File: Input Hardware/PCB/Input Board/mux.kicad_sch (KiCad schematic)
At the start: 40 parts

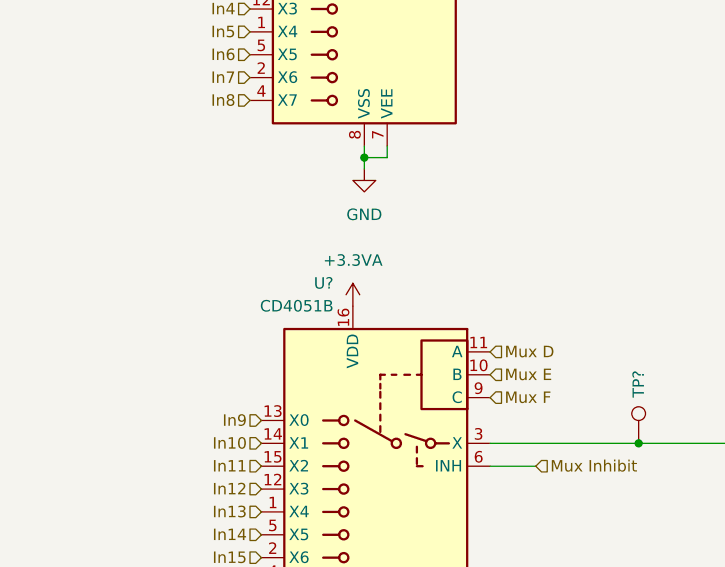
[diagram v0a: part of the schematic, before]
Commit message: Fix footprints
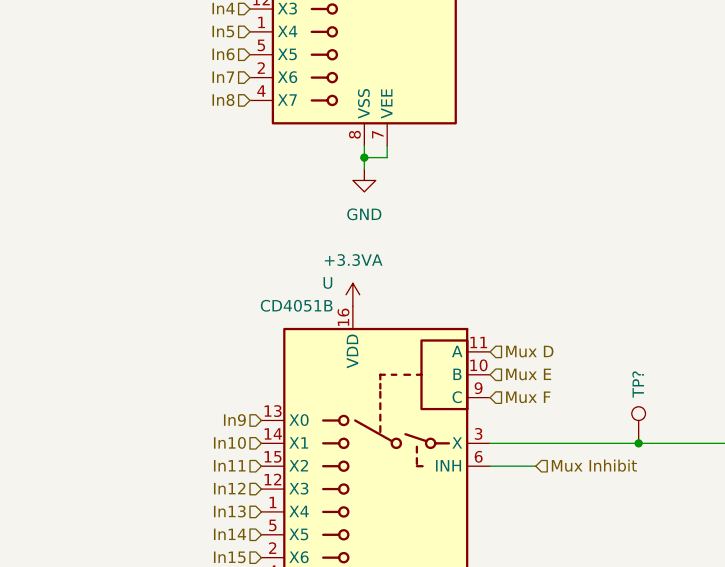
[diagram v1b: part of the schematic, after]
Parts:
- removed U? (x2): CD4051B, symbol Analog_Switch:CD4051B
- added U, U?: CD4051B, Package_SO:SOIC-16_3.9x9.9mm_P1.27mm, symbol Analog_Switch:CD4051B
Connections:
- net +3.3VA: now also U.16 (VDD), U?.16 (VDD)
- net GND: now also U.7 (VEE), U.8 (VSS), U?.7 (VEE), U?.8 (VSS)
- net In1: now also U?.13 (X0)
- net In10: now also U.14 (X1)
- net In11: now also U.15 (X2)
- net In12: now also U.12 (X3)
- net In13: now also U.1 (X4)
- net In14: now also U.5 (X5)
- net In15: now also U.2 (X6)
- net In16: now also U.4 (X7)
- net In2: now also U?.14 (X1)
- net In3: now also U?.15 (X2)
- net In4: now also U?.12 (X3)
- net In5: now also U?.1 (X4)
- net In6: now also U?.5 (X5)
- net In7: now also U?.2 (X6)
- net In8: now also U?.4 (X7)
- net In9: now also U.13 (X0)
- net Mux A: now also U?.11 (A)
- net Mux B: now also U?.10 (B)
- net Mux C: now also U?.9 (C)
- net Mux D: now also U.11 (A)
- net Mux E: now also U.10 (B)
- net Mux F: now also U.9 (C)
- net Mux Inhibit: now also U.6 (INH), U?.6 (INH)
- net at R?.1, TP?.1: now also U?.3 (X)
- net at R?.1, TP?.1: now also U.3 (X)
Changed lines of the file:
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@@
-	)
-	(symbol
-		(lib_id "Analog_Switch:CD4051B")
-		(at 59.69 43.18 0)
-		(mirror y)
-		(unit 1)
-		(exclude_from_sim no)
-		(in_bom yes)
-		(on_board yes)
-		(dnp no)
-		(property "Reference" "U?"
-			(at 55.0067 22.86 0)
-			(effects
-				(font
-					(size 1.27 1.27)
-				)
-				(justify left)
-			)
-		)
-		(property "Value" "CD4051B"
-			(at 55.0067 25.4 0)
-			(effects
-				(font
-					(size 1.27 1.27)
-				)
-				(justify left)
-			)
-		)
-		(property "Footprint" ""
-			(at 55.88 62.23 0)
-			(effects
-				(font
-					(size 1.27 1.27)
-				)
-				(justify left)
-				(hide yes)
-			)
-		)
-		(property "Datasheet" "http://www.ti.com/lit/ds/symlink/cd4052b.pdf"
-			(at 60.198 40.64 0)
-			(effects
-				(font
-					(size 1.27 1.27)
-				)
-				(hide yes)
-			)
-		)
-		(property "Description" "CMOS single 8-channel analog multiplexer demultiplexer, TSSOP-16/DIP-16/SOIC-16"
-			(at 59.69 43.18 0)
-			(effects
-				(font
-					(size 1.27 1.27)
-				)
-				(hide yes)
-			)
-		)
-		(pin "11"
-		)
-		(pin "4"
-		)
-		(pin "5"
-		)
-		(pin "14"
-		)
-		(pin "16"
-		)
-		(pin "7"
-		)
-		(pin "6"
-		)
-		(pin "3"
-		)
-		(pin "9"
-		)
-		(pin "8"
-		)
-		(pin "1"
-		)
-		(pin "10"
-		)
-		(pin "12"
-		)
-		(pin "15"
-		)
-		(pin "13"
-		)
-		(pin "2"
-		)
-		(instances
-			(project "Input Board"
-				(path "/198ad8d1-66e3-4deb-889c-1af2b81e67c3/99a15fca-8895-44e6-9a10-1270216dbd6f"
-					(reference "U?")
-					(unit 1)
-				)
-				(path "/198ad8d1-66e3-4deb-889c-1af2b81e67c3/ccfc9974-2797-4490-9af9-c0259e48d54a"
-					(reference "U?")
-					(unit 1)
-				)
-			)
-		)
 	)
 	(symbol
@@
 	)
 	(symbol
+		(lib_id "Analog_Switch:CD4051B")
+		(at 59.69 43.18 0)
+		(mirror y)
+		(unit 1)
+		(exclude_from_sim no)
+		(in_bom yes)
+		(on_board yes)
+		(dnp no)
+		(property "Reference" "U?"
+			(at 55.0067 22.86 0)
+			(effects
+				(font
+					(size 1.27 1.27)
+				)
+				(justify left)
+			)
+		)
+		(property "Value" "CD4051B"
+			(at 55.0067 25.4 0)
+			(effects
+				(font
+					(size 1.27 1.27)
+				)
+				(justify left)
+			)
+		)
+		(property "Footprint" "Package_SO:SOIC-16_3.9x9.9mm_P1.27mm"
+			(at 55.88 62.23 0)
+			(effects
+				(font
+					(size 1.27 1.27)
+				)
+				(justify left)
+				(hide yes)
+			)
+		)
+		(property "Datasheet" "http://www.ti.com/lit/ds/symlink/cd4052b.pdf"
+			(at 60.198 40.64 0)
+			(effects
+				(font
+					(size 1.27 1.27)
+				)
+				(hide yes)
+			)
+		)
+		(property "Description" "CMOS single 8-channel analog multiplexer demultiplexer, TSSOP-16/DIP-16/SOIC-16"
+			(at 59.69 43.18 0)
+			(effects
+				(font
+					(size 1.27 1.27)
+				)
+				(hide yes)
+			)
+		)
+		(pin "8"
+		)
+		(pin "14"
+		)
+		(pin "13"
+		)
+		(pin "4"
+		)
+		(pin "2"
+		)
+		(pin "9"
+		)
+		(pin "10"
+		)
+		(pin "1"
+		)
+		(pin "15"
+		)
+		(pin "6"
+		)
+		(pin "16"
+		)
+		(pin "3"
+		)
+		(pin "7"
+		)
+		(pin "12"
+		)
+		(pin "5"
+		)
+		(pin "11"
+		)
+		(instances
+			(project "Input Board"
+				(path "/198ad8d1-66e3-4deb-889c-1af2b81e67c3/99a15fca-8895-44e6-9a10-1270216dbd6f"
+					(reference "U?")
+					(unit 1)
+				)
+				(path "/198ad8d1-66e3-4deb-889c-1af2b81e67c3/ccfc9974-2797-4490-9af9-c0259e48d54a"
+					(reference "U?")
+					(unit 1)
+				)
+			)
+		)
+	)
+	(symbol
 		(lib_id "power:+3.3VA")
 		(at 58.42 78.74 0)
@@
 	)
 	(symbol
+		(lib_id "Analog_Switch:CD4051B")
+		(at 60.96 96.52 0)
+		(mirror y)
+		(unit 1)
+		(exclude_from_sim no)
+		(in_bom yes)
+		(on_board yes)
+		(dnp no)
+		(property "Reference" "U"
+			(at 56.2767 76.2 0)
+			(effects
+				(font
+					(size 1.27 1.27)
+				)
+				(justify left)
+			)
+		)
+		(property "Value" "CD4051B"
+			(at 56.2767 78.74 0)
+			(effects
+				(font
+					(size 1.27 1.27)
+				)
+				(justify left)
+			)
+		)
+		(property "Footprint" "Package_SO:SOIC-16_3.9x9.9mm_P1.27mm"
+			(at 57.15 115.57 0)
+			(effects
+				(font
+					(size 1.27 1.27)
+				)
+				(justify left)
+				(hide yes)
+			)
+		)
+		(property "Datasheet" "http://www.ti.com/lit/ds/symlink/cd4052b.pdf"
+			(at 61.468 93.98 0)
+			(effects
+				(font
+					(size 1.27 1.27)
+				)
+				(hide yes)
+			)
+		)
+		(property "Description" "CMOS single 8-channel analog multiplexer demultiplexer, TSSOP-16/DIP-16/SOIC-16"
+			(at 60.96 96.52 0)
+			(effects
+				(font
+					(size 1.27 1.27)
+				)
+				(hide yes)
+			)
+		)
+		(pin "8"
+		)
+		(pin "14"
+		)
+		(pin "13"
+		)
+		(pin "4"
+		)
+		(pin "2"
+		)
+		(pin "9"
+		)
+		(pin "10"
+		)
+		(pin "1"
+		)
+		(pin "15"
+		)
+		(pin "6"
+		)
+		(pin "16"
+		)
+		(pin "3"
+		)
+		(pin "7"
+		)
+		(pin "12"
+		)
+		(pin "5"
+		)
+		(pin "11"
+		)
+		(instances
+			(project ""
+				(path "/198ad8d1-66e3-4deb-889c-1af2b81e67c3/ccfc9974-2797-4490-9af9-c0259e48d54a"
+					(reference "U?")
+					(unit 1)
+				)
+			)
+		)
+	)
+	(symbol
 		(lib_id "Device:R")
 		(at 149.86 49.53 0)
@@
 					(unit 1)
 				)
-			)
-		)
-	)
-	(symbol
-		(lib_id "Analog_Switch:CD4051B")
-		(at 60.96 96.52 0)
-		(mirror y)
-		(unit 1)
-		(exclude_from_sim no)
-		(in_bom yes)
-		(on_board yes)
-		(dnp no)
-		(property "Reference" "U?"
-			(at 56.2767 76.2 0)
-			(effects
-				(font
-					(size 1.27 1.27)
-				)
-				(justify left)
-			)
-		)
-		(property "Value" "CD4051B"
-			(at 56.2767 78.74 0)
-			(effects
-				(font
-					(size 1.27 1.27)
-				)
-				(justify left)
-			)
-		)
-		(property "Footprint" ""
-			(at 57.15 115.57 0)
-			(effects
-				(font
-					(size 1.27 1.27)
-				)
-				(justify left)
-				(hide yes)
-			)
-		)
-		(property "Datasheet" "http://www.ti.com/lit/ds/symlink/cd4052b.pdf"
-			(at 61.468 93.98 0)
-			(effects
-				(font
-					(size 1.27 1.27)
-				)
-				(hide yes)
-			)
-		)
-		(property "Description" "CMOS single 8-channel analog multiplexer demultiplexer, TSSOP-16/DIP-16/SOIC-16"
-			(at 60.96 96.52 0)
-			(effects
-				(font
-					(size 1.27 1.27)
-				)
-				(hide yes)
-			)
-		)
-		(pin "11"
-		)
-		(pin "4"
-		)
-		(pin "5"
-		)
-		(pin "14"
-		)
-		(pin "16"
-		)
-		(pin "7"
-		)
-		(pin "6"
-		)
-		(pin "3"
-		)
-		(pin "9"
-		)
-		(pin "8"
-		)
-		(pin "1"
-		)
-		(pin "10"
-		)
-		(pin "12"
-		)
-		(pin "15"
-		)
-		(pin "13"
-		)
-		(pin "2"
-		)
-		(instances
-			(project "Input Board"
-				(path "/198ad8d1-66e3-4deb-889c-1af2b81e67c3/99a15fca-8895-44e6-9a10-1270216dbd6f"
-					(reference "U?")
-					(unit 1)
-				)
-				(path "/198ad8d1-66e3-4deb-889c-1af2b81e67c3/ccfc9974-2797-4490-9af9-c0259e48d54a"
-					(reference "U?")
-					(unit 1)
-				)

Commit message: Fix files idc
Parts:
- gave numbers to parts that had none: 35
- renumbered U to U703

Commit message: Filter Amplifier Layout
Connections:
- net In10: now also U703.12 (X3); no longer U703.14 (X1)
- net In12: now also U703.14 (X1); no longer U703.12 (X3)
- net In13: now also U703.4 (X7); no longer U703.1 (X4)
- net In16: now also U703.1 (X4); no longer U703.4 (X7)
- net In2: now also U702.12 (X3); no longer U702.14 (X1)
- net In4: now also U702.14 (X1); no longer U702.12 (X3)
- net In5: now also U702.4 (X7); no longer U702.1 (X4)
- net In8: now also U702.1 (X4); no longer U702.4 (X7)
- net at R715.1, R716.2: now also U701.9 (-); no longer U701.13 (-)
- net at R712.1, R715.2, R718.2: now also U701.8; no longer U701.14
- net at C711.2, R710.2: now also U701.10 (+); no longer U701.12 (+)
- net at R707.1, R708.2: now also U701.13 (-); no longer U701.9 (-)
- net at C707.2, C709.1, R707.2: now also U701.14; no longer U701.8
- net at C705.1, R704.2: now also U701.12 (+); no longer U701.10 (+)
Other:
- moved on the sheet: U701C, U701D
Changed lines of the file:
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@@
 	(hierarchical_label "In10"
 		(shape input)
-		(at 48.26 93.98 180)
+		(at 48.26 99.06 180)
 		(effects
 			(font
@@
 	(hierarchical_label "In16"
 		(shape input)
-		(at 48.26 109.22 180)
+		(at 48.26 101.6 180)
 		(effects
 			(font
@@
 	(hierarchical_label "In4"
 		(shape input)
-		(at 46.99 45.72 180)
+		(at 46.99 40.64 180)
 		(effects
 			(font
@@
 	(hierarchical_label "In2"
 		(shape input)
-		(at 46.99 40.64 180)
+		(at 46.99 45.72 180)
 		(effects
 			(font
@@
 	(hierarchical_label "In8"
 		(shape input)
-		(at 46.99 55.88 180)
+		(at 46.99 48.26 180)
 		(effects
 			(font
@@
 	(hierarchical_label "In12"
 		(shape input)
-		(at 48.26 99.06 180)
+		(at 48.26 93.98 180)
 		(effects
 			(font
@@
 	(hierarchical_label "In13"
 		(shape input)
-		(at 48.26 101.6 180)
+		(at 48.26 109.22 180)
 		(effects
 			(font
@@
 	(hierarchical_label "In5"
 		(shape input)
-		(at 46.99 48.26 180)
+		(at 46.99 55.88 180)
 		(effects
 			(font
@@
 	(symbol
 		(lib_id "Device:Opamp_Quad")
-		(at 140.97 96.52 0)
+		(at 207.01 96.52 0)
 		(unit 3)
 		(exclude_from_sim no)
@@
 		(fields_autoplaced yes)
 		(property "Reference" "U701"
-			(at 140.97 86.36 0)
+			(at 207.01 86.36 0)
 			(effects
 				(font
@@
 		)
 		(property "Value" "ADA4891"
-			(at 140.97 88.9 0)
+			(at 207.01 88.9 0)
 			(effects
 				(font
@@
 		)
 		(property "Footprint" "Package_SO:SOIC-14_3.9x8.7mm_P1.27mm"
-			(at 153.67 96.52 0)
+			(at 219.71 96.52 0)
 			(effects
 				(font
@@
 		)
 		(property "Datasheet" "~"
-			(at 140.97 96.52 0)
+			(at 207.01 96.52 0)
 			(effects
 				(font
@@
 		)
 		(property "Description" "Quad operational amplifier"
-			(at 140.97 96.52 0)
+			(at 207.01 96.52 0)
 			(effects
 				(font
@@
 		)
 		(property "Sim.Library" "${KICAD9_SYMBOL_DIR}/Simulation_SPICE.sp"
-			(at 140.97 96.52 0)
+			(at 207.01 96.52 0)
 			(effects
 				(font
@@
 		)
 		(property "Sim.Name" "kicad_builtin_opamp_quad"
-			(at 140.97 96.52 0)
+			(at 207.01 96.52 0)
 			(effects
 				(font
@@
 		)
 		(property "Sim.Device" "SUBCKT"
-			(at 140.97 96.52 0)
+			(at 207.01 96.52 0)
 			(effects
 				(font
@@
 		)
 		(property "Sim.Pins" "1=out1 2=in1- 3=in1+ 4=vcc 5=in2+ 6=in2- 7=out2 8=out3 9=in3- 10=in3+ 11=vee 12=in4+ 13=in4- 14=out4"
-			(at 140.97 96.52 0)
+			(at 207.01 96.52 0)
 			(effects
 				(font
@@
 	(symbol
 		(lib_id "Device:Opamp_Quad")
-		(at 207.01 96.52 0)
+		(at 140.97 96.52 0)
 		(unit 4)
 		(exclude_from_sim no)
@@
 		(fields_autoplaced yes)
 		(property "Reference" "U701"
-			(at 207.01 86.36 0)
+			(at 140.97 86.36 0)
 			(effects
 				(font
@@
 		)
 		(property "Value" "ADA4891"
-			(at 207.01 88.9 0)
+			(at 140.97 88.9 0)
 			(effects
 				(font
@@
 		)
 		(property "Footprint" "Package_SO:SOIC-14_3.9x8.7mm_P1.27mm"
-			(at 219.71 96.52 0)
+			(at 153.67 96.52 0)
 			(effects
 				(font
@@
 		)
 		(property "Datasheet" "~"
-			(at 207.01 96.52 0)
+			(at 140.97 96.52 0)
 			(effects
 				(font
@@
 		)
 		(property "Description" "Quad operational amplifier"
-			(at 207.01 96.52 0)
+			(at 140.97 96.52 0)
 			(effects
 				(font
@@
 		)
 		(property "Sim.Library" "${KICAD9_SYMBOL_DIR}/Simulation_SPICE.sp"
-			(at 207.01 96.52 0)
+			(at 140.97 96.52 0)
 			(effects
 				(font
@@
 		)
 		(property "Sim.Name" "kicad_builtin_opamp_quad"
-			(at 207.01 96.52 0)
+			(at 140.97 96.52 0)
 			(effects
 				(font
@@
 		)
 		(property "Sim.Device" "SUBCKT"
-			(at 207.01 96.52 0)
+			(at 140.97 96.52 0)
 			(effects
 				(font
@@
 		)
 		(property "Sim.Pins" "1=out1 2=in1- 3=in1+ 4=vcc 5=in2+ 6=in2- 7=out2 8=out3 9=in3- 10=in3+ 11=vee 12=in4+ 13=in4- 14=out4"
-			(at 207.01 96.52 0)
-			(effects
-				(font
+			(at 140.97 96.52 0)
+			(effects
+				(font

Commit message: Layout
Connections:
- net GNDA is gone; now on net GND: C703.2, U701.11 (V-)
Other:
- moved on the sheet: C703
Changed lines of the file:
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@@
 	)
 	(junction
-		(at 66.04 179.07)
-		(diameter 0)
-		(color 0 0 0 0)
-	)
-	(junction
 		(at 189.23 93.98)
 		(diameter 0)
@@
 	)
 	(junction
+		(at 62.23 179.07)
+		(diameter 0)
+		(color 0 0 0 0)
+	)
+	(junction
 		(at 175.26 40.64)
 		(diameter 0)
@@
 	)
 	(junction
-		(at 242.57 96.52)
+		(at 62.23 163.83)
 		(diameter 0)
 		(color 0 0 0 0)
 	)
 	(junction
-		(at 121.92 40.64)
+		(at 242.57 96.52)
 		(diameter 0)
 		(color 0 0 0 0)
 	)
 	(junction
-		(at 176.53 93.98)
+		(at 121.92 40.64)
 		(diameter 0)
 		(color 0 0 0 0)
 	)
 	(junction
-		(at 66.04 163.83)
+		(at 176.53 93.98)
 		(diameter 0)
 		(color 0 0 0 0)
@@
 	(wire
 		(pts
-			(xy 74.93 167.64) (xy 74.93 163.83)
+			(xy 68.58 167.64) (xy 68.58 163.83)
 		)
 		(stroke
@@
 	(wire
 		(pts
-			(xy 55.88 179.07) (xy 66.04 179.07)
-		)
-		(stroke
-			(width 0)
-			(type default)
-		)
-	)
-	(wire
-		(pts
 			(xy 60.96 115.57) (xy 63.5 115.57)
 		)
@@
 	(wire
 		(pts
-			(xy 74.93 179.07) (xy 74.93 175.26)
+			(xy 68.58 179.07) (xy 68.58 175.26)
 		)
 		(stroke
@@
 	(wire
 		(pts
-			(xy 66.04 163.83) (xy 74.93 163.83)
-		)
-		(stroke
-			(width 0)
-			(type default)
-		)
-	)
-	(wire
-		(pts
 			(xy 130.81 54.61) (xy 149.86 54.61)
 		)
@@
 	(wire
 		(pts
-			(xy 66.04 179.07) (xy 74.93 179.07)
+			(xy 55.88 179.07) (xy 62.23 179.07)
 		)
 		(stroke
@@
 	(wire
 		(pts
+			(xy 62.23 179.07) (xy 68.58 179.07)
+		)
+		(stroke
+			(width 0)
+			(type default)
+		)
+	)
+	(wire
+		(pts
 			(xy 149.86 27.94) (xy 149.86 43.18)
 		)
@@
 	(wire
 		(pts
+			(xy 62.23 163.83) (xy 68.58 163.83)
+		)
+		(stroke
+			(width 0)
+			(type default)
+		)
+	)
+	(wire
+		(pts
 			(xy 172.72 40.64) (xy 175.26 40.64)
 		)
@@
 	(wire
 		(pts
-			(xy 55.88 163.83) (xy 66.04 163.83)
+			(xy 55.88 163.83) (xy 62.23 163.83)
 		)
 		(stroke
@@
 	(symbol
 		(lib_id "power:+3.3VA")
-		(at 66.04 163.83 0)
+		(at 62.23 163.83 0)
 		(unit 1)
 		(exclude_from_sim no)
@@
 		(fields_autoplaced yes)
 		(property "Reference" "#PWR0709"
-			(at 66.04 167.64 0)
+			(at 62.23 167.64 0)
 			(effects
 				(font
@@
 		)
 		(property "Value" "+3.3VA"
-			(at 66.04 158.75 0)
+			(at 62.23 158.75 0)
 			(effects
 				(font
@@
 		)
 		(property "Footprint" ""
-			(at 66.04 163.83 0)
+			(at 62.23 163.83 0)
 			(effects
 				(font
@@
 		)
 		(property "Datasheet" ""
-			(at 66.04 163.83 0)
+			(at 62.23 163.83 0)
 			(effects
 				(font
@@
 		)
 		(property "Description" "Power symbol creates a global label with name \"+3.3VA\""
-			(at 66.04 163.83 0)
+			(at 62.23 163.83 0)
 			(effects
 				(font
@@
 	(symbol
 		(lib_id "Device:C")
-		(at 74.93 171.45 0)
+		(at 68.58 171.45 0)
 		(unit 1)
 		(exclude_from_sim no)
@@
 		(fields_autoplaced yes)
 		(property "Reference" "C703"
-			(at 78.74 170.1799 0)
+			(at 72.39 170.1799 0)
 			(effects
 				(font
@@
 		)
 		(property "Value" "100n"
-			(at 78.74 172.7199 0)
+			(at 72.39 172.7199 0)
 			(effects
 				(font
@@
 		)
 		(property "Footprint" "Capacitor_SMD:C_0603_1608Metric"
-			(at 75.8952 175.26 0)
+			(at 69.5452 175.26 0)
 			(effects
 				(font
@@
 		)
 		(property "Datasheet" "~"
-			(at 74.93 171.45 0)
+			(at 68.58 171.45 0)
 			(effects
 				(font
@@
 		)
 		(property "Description" "Unpolarized capacitor"
-			(at 74.93 171.45 0)
+			(at 68.58 171.45 0)
 			(effects
 				(font
@@
 	)
 	(symbol
-		(lib_id "power:GNDA")
-		(at 66.04 179.07 0)
-		(unit 1)
-		(exclude_from_sim no)
-		(in_bom yes)
-		(on_board yes)
-		(dnp no)
-		(fields_autoplaced yes)
-		(property "Reference" "#PWR0710"
-			(at 66.04 185.42 0)
-			(effects
-				(font
-					(size 1.27 1.27)
-				)
-				(hide yes)
-			)
-		)
-		(property "Value" "GNDA"
-			(at 66.04 184.15 0)
-			(effects
-				(font
-					(size 1.27 1.27)
-				)
-			)
-		)
-		(property "Footprint" ""
-			(at 66.04 179.07 0)
-			(effects
-				(font
-					(size 1.27 1.27)
-				)
-				(hide yes)
-			)
-		)
-		(property "Datasheet" ""
-			(at 66.04 179.07 0)
-			(effects
-				(font
-					(size 1.27 1.27)
-				)
-				(hide yes)
-			)
-		)
-		(property "Description" "Power symbol creates a global label with name \"GNDA\" , analog ground"
-			(at 66.04 179.07 0)
-			(effects
-				(font
-					(size 1.27 1.27)
-				)
-				(hide yes)
-			)
-		)
-		(pin "1"
-		)
-		(instances
-			(project "Input Board"
-				(path "/198ad8d1-66e3-4deb-889c-1af2b81e67c3/99a15fca-8895-44e6-9a10-1270216dbd6f"
-					(reference "#PWR0810")
-					(unit 1)
-				)
-				(path "/198ad8d1-66e3-4deb-889c-1af2b81e67c3/ccfc9974-2797-4490-9af9-c0259e48d54a"
-					(reference "#PWR0710")
-					(unit 1)
-				)
-			)
-		)
-	)
-	(symbol
 		(lib_id "Device:R")
 		(at 151.13 102.87 0)
@@
 					(unit 1)
 				)
+			)
+		)
+	)
+	(symbol
+		(lib_id "power:GND")
+		(at 62.23 179.07 0)
+		(unit 1)
+		(exclude_from_sim no)
+		(in_bom yes)
+		(on_board yes)
+		(dnp no)
+		(fields_autoplaced yes)
+		(property "Reference" "#PWR089"
+			(at 62.23 185.42 0)
+			(effects
+				(font
+					(size 1.27 1.27)
+				)
+				(hide yes)
+			)
+		)
+		(property "Value" "GND"
+			(at 62.23 184.15 0)
+			(effects
+				(font
+					(size 1.27 1.27)
+				)
+			)
+		)
+		(property "Footprint" ""
+			(at 62.23 179.07 0)
+			(effects
+				(font
+					(size 1.27 1.27)
+				)
+				(hide yes)
+			)
+		)
+		(property "Datasheet" ""
+			(at 62.23 179.07 0)
+			(effects
+				(font
+					(size 1.27 1.27)
+				)
+				(hide yes)
+			)
+		)
+		(property "Description" "Power symbol creates a global label with name \"GND\" , ground"
+			(at 62.23 179.07 0)
+			(effects
+				(font
+					(size 1.27 1.27)
+				)
+				(hide yes)
+			)
+		)
+		(pin "1"
+		)
+		(instances
+			(project "Input Board"
+				(path "/198ad8d1-66e3-4deb-889c-1af2b81e67c3/99a15fca-8895-44e6-9a10-1270216dbd6f"
+					(reference "#PWR090")
+					(unit 1)
+				)
+				(path "/198ad8d1-66e3-4deb-889c-1af2b81e67c3/ccfc9974-2797-4490-9af9-c0259e48d54a"
+					(reference "#PWR089")
+					(unit 1)
+				)

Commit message: sims and other crap
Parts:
- C706, C707: value 39p -> 33p
- C708, C709, C710, C711: value 56p -> 39p
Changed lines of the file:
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@@
 			)
 		)
-		(property "Value" "56p"
+		(property "Value" "39p"
 			(at 182.88 88.9 90)
 			(effects
@@
 			)
 		)
-		(property "Value" "39p"
+		(property "Value" "33p"
 			(at 133.35 76.2 90)
 			(effects
@@
 			)
 		)
-		(property "Value" "56p"
+		(property "Value" "39p"
 			(at 170.18 88.9 90)
 			(effects
@@
 			)
 		)
-		(property "Value" "39p"
+		(property "Value" "33p"
 			(at 132.08 22.86 90)
 			(effects
@@
 			)
 		)
-		(property "Value" "56p"
+		(property "Value" "39p"
 			(at 168.91 35.56 90)
 			(effects
@@
 			)
 		)
-		(property "Value" "56p"
+		(property "Value" "39p"
 			(at 181.61 35.56 90)
 			(effects
